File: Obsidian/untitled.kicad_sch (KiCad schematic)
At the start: 72 parts, among them U12 LP5951MF-3.0/NOPB, U13 LM336M-2.5, U14 DAC8550IDGK, U15 DAC8550IDGK, U16 CDCM61004RHB, U3 Si5351A-B-GT, Y1 OSC_25MHZ_RAKON_IVT3205CR, Y2 VM53S3-25.000-2.5/-30+75, Y3 OSC_20MHZ_IQD_LFVCXO026156, Y6 XTAL_25MHZ_TXC_8Y-25.000MAAJ-T

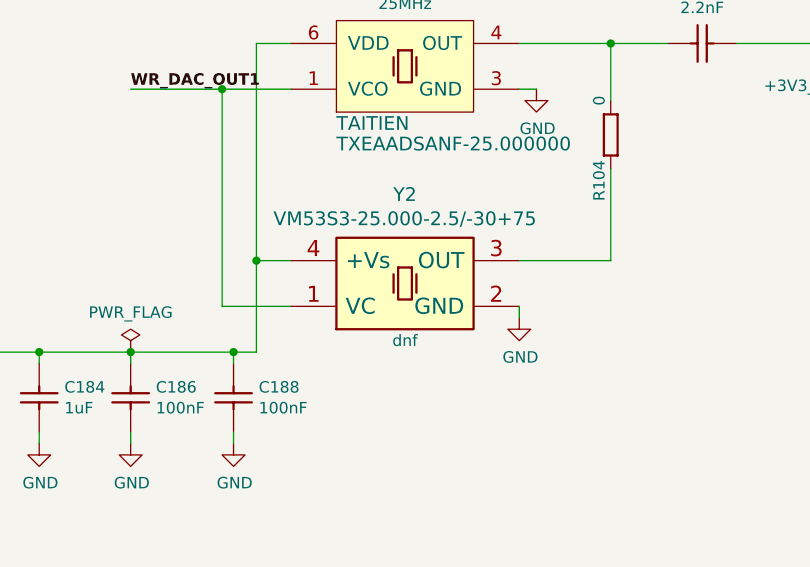
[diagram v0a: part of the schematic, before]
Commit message: update with available components on LCSC
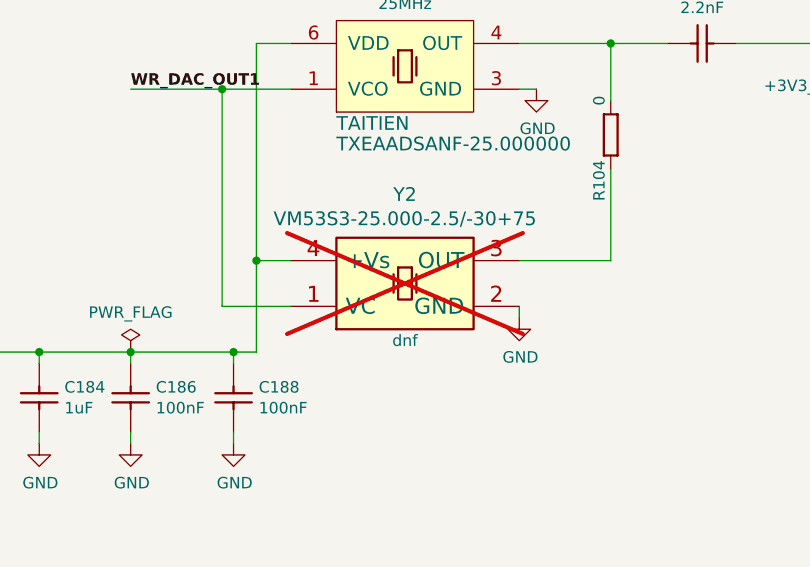
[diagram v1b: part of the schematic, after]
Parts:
- C182, C184, C207: LCSC (none) -> C29266
- C183, C185, C186, C188, C189, C190, C191, C194, C196, C197, C198, C206, C208, C209, C210, C211, C212, C215: LCSC (none) -> C190187
- C187, C192, C195, C199, C200, C201, C203: LCSC (none) -> C59461
- C193: LCSC (none) -> C1531
- C202, C204, C205, C213, C214, C248: LCSC (none) -> C110251
- L17, L18, L20: FT Rotation Offset (none) -> 0; LCSC (none) -> C113030
- R102, R103, R120, R121, R99: LCSC (none) -> C25094
- R104, R105, R106, R107, R108, R109, R110, R111, R112: LCSC (none) -> C106231
- R113, R116: LCSC (none) -> C351694
- R115, R117: LCSC (none) -> C413063
- R118, R119: LCSC (none) -> C114764
- R159: LCSC (none) -> C25111
- R162: LCSC (none) -> C25776
- R163, R176: LCSC (none) -> C60490
- U12: FT Rotation Offset (none) -> 270; LCSC (none) -> C2868982
- U13: FT Rotation Offset (none) -> 270; LCSC (none) -> C507207
- U14, U15: FT Rotation Offset (none) -> 270; LCSC (none) -> C524800
- U16: FT Rotation Offset (none) -> 0; LCSC (none) -> C524817
- U3: FT Rotation Offset (none) -> 0; LCSC (none) -> C504891
- Y1: LCSC (none) -> C52954962
- Y2: now not fitted
- Y3: FT Rotation Offset (none) -> 190; LCSC (none) -> C21547610
- Y6: FT Rotation Offset (none) -> 270; LCSC (none) -> C648942

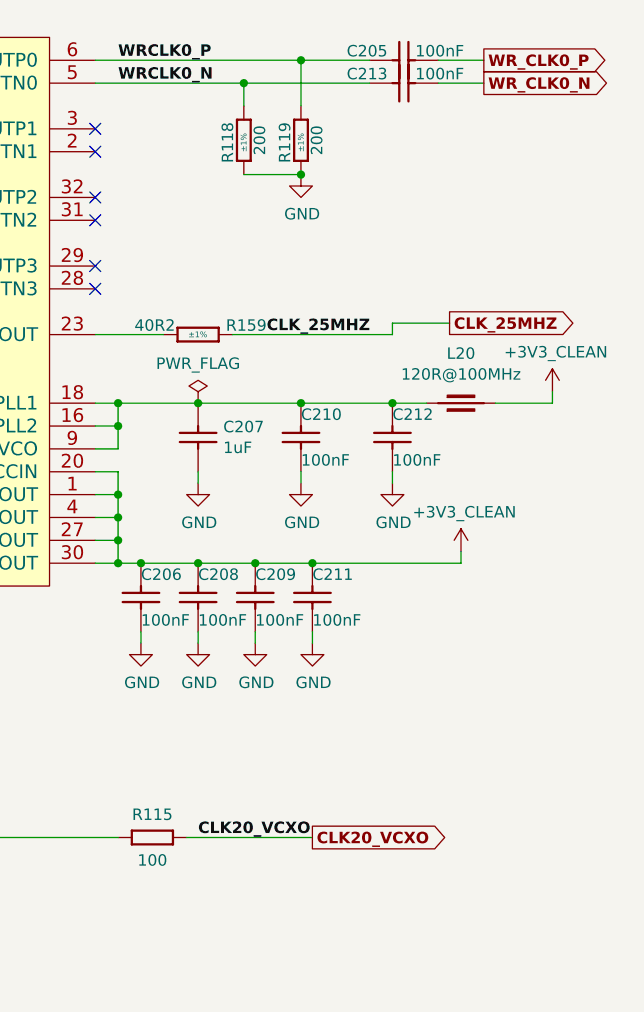
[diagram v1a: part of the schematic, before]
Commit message: adding wago
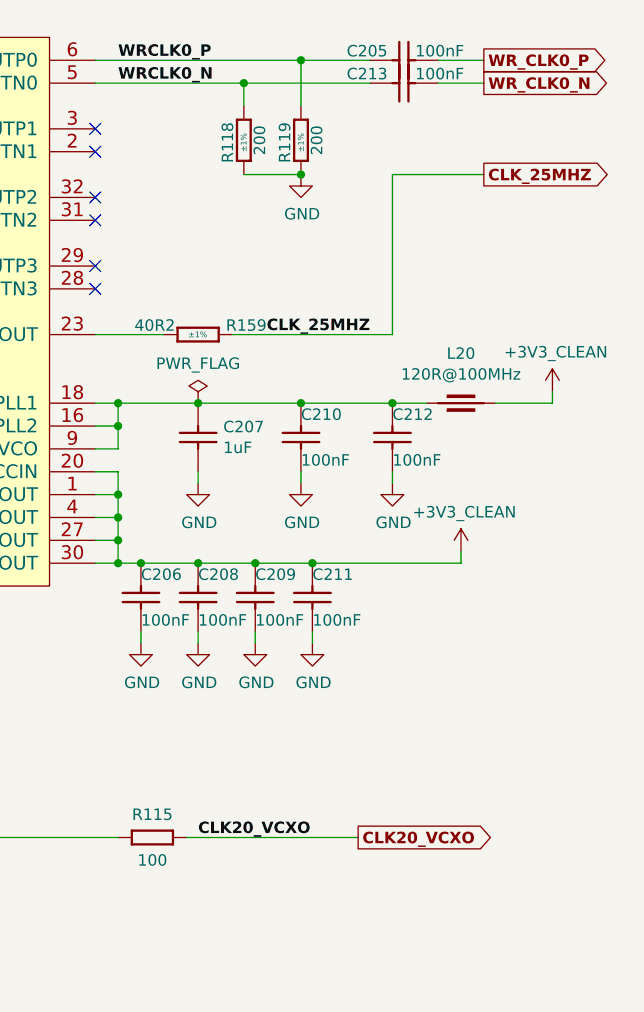
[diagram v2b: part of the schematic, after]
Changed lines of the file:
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@@
 	(wire
 		(pts
-			(xy 237.49 111.76) (xy 251.46 111.76)
+			(xy 237.49 111.76) (xy 256.54 111.76)
 		)
 		(stroke
@@
 	(wire
 		(pts
-			(xy 260.35 54.61) (xy 266.7 54.61)
+			(xy 260.35 38.1) (xy 270.51 38.1)
 		)
 		(stroke
@@
 	(wire
 		(pts
-			(xy 260.35 55.88) (xy 260.35 54.61)
+			(xy 260.35 55.88) (xy 260.35 38.1)
 		)
 		(stroke
@@
 	(global_label "CLK20_VCXO"
 		(shape output)
-		(at 251.46 111.76 0)
+		(at 256.54 111.76 0)
 		(fields_autoplaced yes)
 		(effects
@@
 		)
 		(property "Intersheetrefs" "${INTERSHEET_REFS}"
-			(at 266.7745 111.76 0)
+			(at 271.8545 111.76 0)
 			(effects
 				(font
@@
 	(global_label "CLK_25MHZ"
 		(shape output)
-		(at 266.7 54.61 0)
+		(at 270.51 38.1 0)
 		(fields_autoplaced yes)
 		(effects
@@
 		)
 		(property "Intersheetrefs" "${INTERSHEET_REFS}"
-			(at 281.1073 54.61 0)
+			(at 284.9173 38.1 0)
 			(effects
 				(font
@@
 			)
 		)
+	)
+	(rule_area
+		(polyline
+			(pts
+				(xy 269.24 22.86) (xy 269.24 41.91) (xy 284.48 41.91) (xy 284.48 22.86)
+			)
+			(stroke
+				(width 0)
+				(type dash)
+			)
+			(fill
+				(type none)
+			)
+		)
+	)
+	(rule_area
+		(polyline
+			(pts
+				(xy 255.27 107.95) (xy 255.27 163.83) (xy 274.32 163.83) (xy 274.32 107.95)
+			)
+			(stroke
+				(width 0)
+				(type dash)
+			)
+			(fill
+				(type none)
+			)
+		)
+	)
+	(netclass_flag ""
+		(length 2.54)
+		(shape round)
+		(at 264.16 107.95 0)
+		(fields_autoplaced yes)
+		(effects
+			(font
+				(size 1.27 1.27)
+			)
+			(justify left bottom)
+		)
+		(property "Netclass" "CLK"
+			(at 264.8585 105.41 0)
+			(effects
+				(font
+					(size 1.27 1.27)
+				)
+				(justify left)
+			)
+		)
+		(property "Component Class" ""
+			(at -49.53 72.39 0)
+			(effects
+				(font
+					(size 1.27 1.27)
+					(italic yes)
+				)
+			)
+		)
+	)
+	(netclass_flag ""
+		(length 2.54)
+		(shape round)
+		(at 276.86 22.86 0)
+		(fields_autoplaced yes)
+		(effects
+			(font
+				(size 1.27 1.27)
+			)
+			(justify left bottom)
+		)
+		(property "Netclass" "CLK"
+			(at 277.5585 20.32 0)
+			(effects
+				(font
+					(size 1.27 1.27)
+				)
+				(justify left)
+			)
+		)
+		(property "Component Class" ""
+			(at -36.83 -12.7 0)
+			(effects
+				(font
+					(size 1.27 1.27)
+					(italic yes)
+				)
+			)
+		)

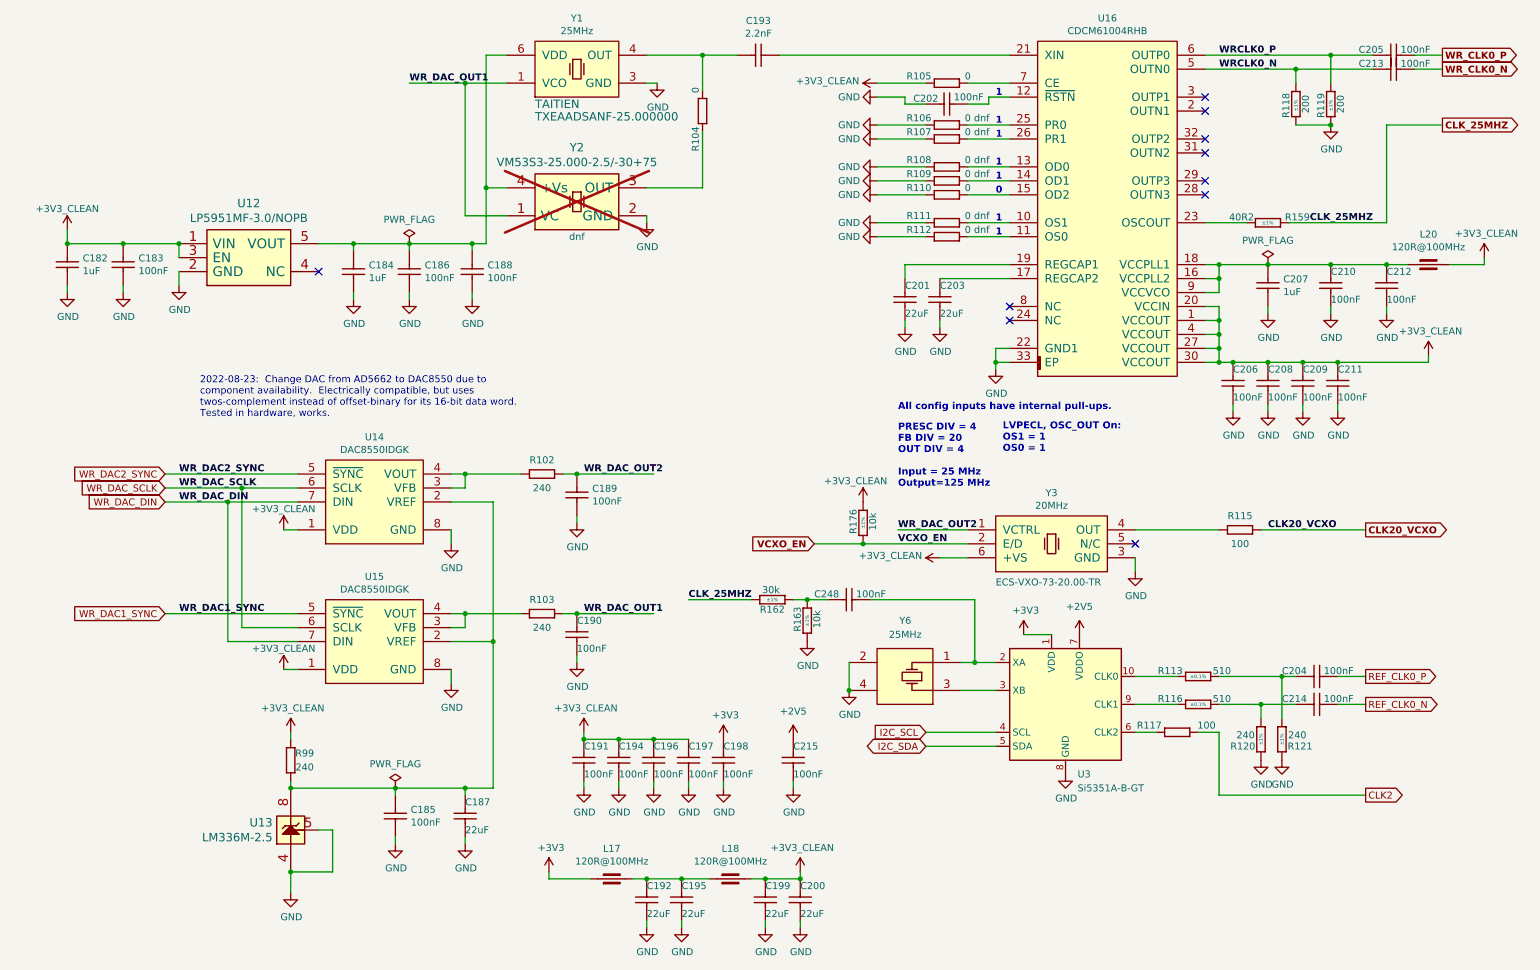
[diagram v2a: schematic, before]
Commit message: replacing global label with hierarchical label
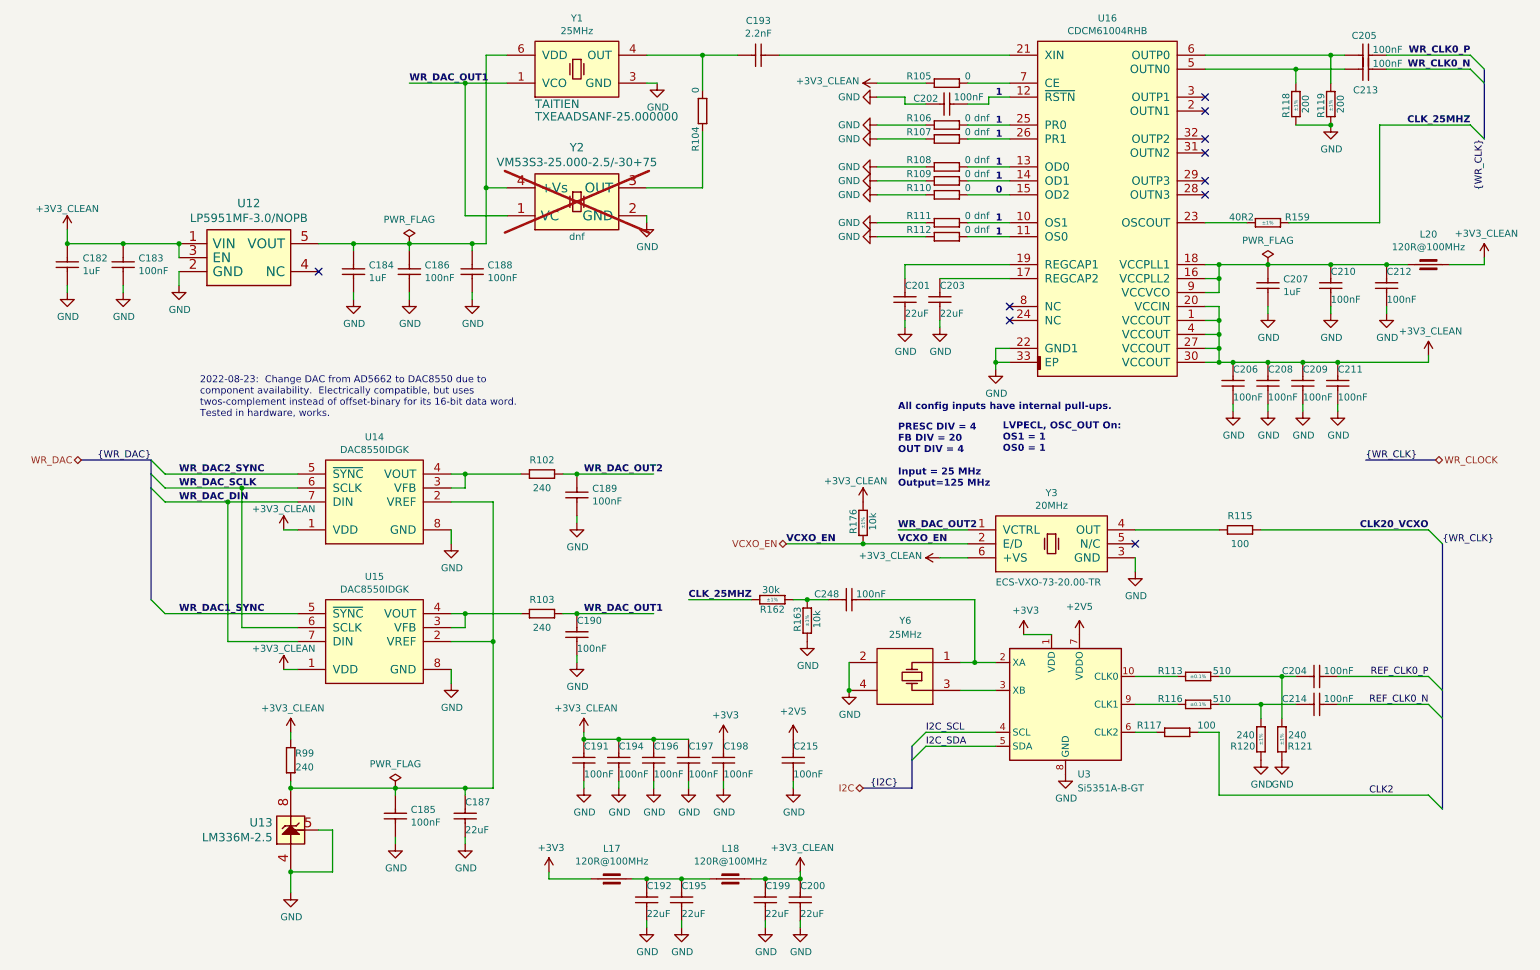
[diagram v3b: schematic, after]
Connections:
- net WRCLK0_N: no longer names the net of C213.2, R118.1, U16.5 (OUTN0)
- net WRCLK0_P: no longer names the net of C205.2, R119.1, U16.6 (OUTP0)
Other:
- moved on the sheet: C205, C213

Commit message: Adding symbol library
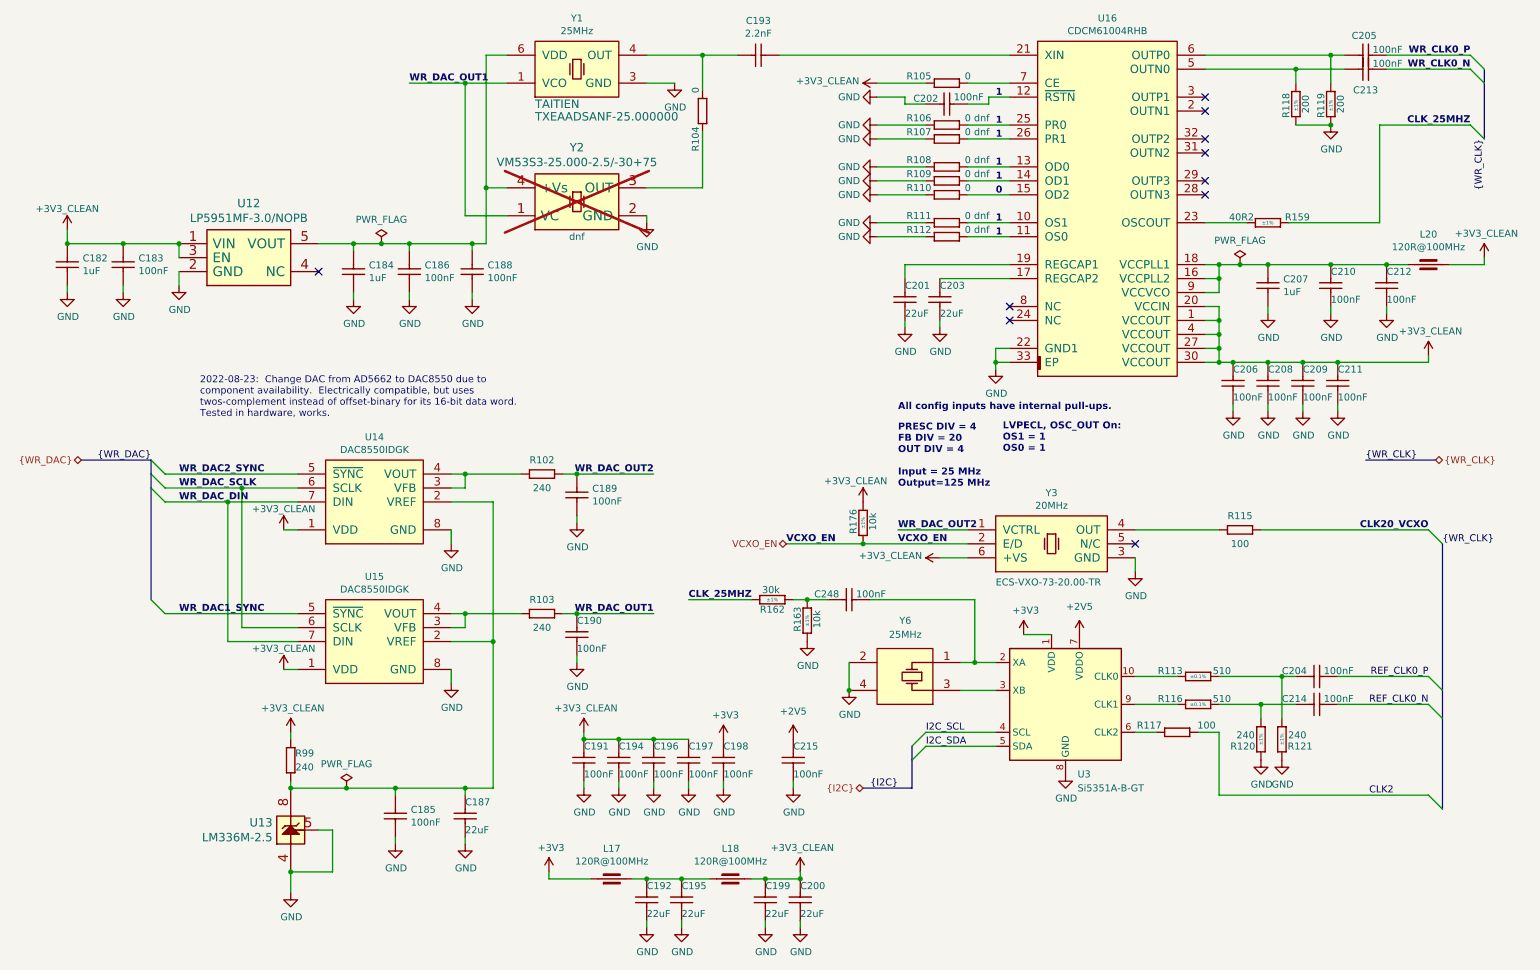
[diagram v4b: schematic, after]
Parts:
- C182, C184, C207: symbol Capacitors_SMD:CC0402_1UF_16V_10%_X5R -> Library_Symbol:CC0402_1UF_16V_10%_X5R
- C183, C185, C186, C188, C189, C190, C191, C194, C196, C197, C198, C206, C208, C209, C210, C211, C212, C215: symbol Capacitors_SMD:CC0201_100NF_6.3V_10%_X5R -> Library_Symbol:CC0201_100NF_6.3V_10%_X5R
- C187, C192, C195, C199, C200, C201, C203: symbol Capacitors_SMD:CC0603_22UF_6.3V_20%_X5R -> Library_Symbol:CC0603_22UF_6.3V_20%_X5R
- C193: symbol Capacitors_SMD:CC0402_2.2NF_50V_10%_X7R -> Library_Symbol:CC0402_2.2NF_50V_10%_X7R
- C202, C204, C205, C213, C214, C248: symbol Capacitors SMD:CC0402_100NF_50V_10%_X7R -> Library_Symbol:CC0402_100NF_50V_10%_X7R
- L17, L18, L20: symbol Inductors_SMD:IND0603_MURATA_BLM18SG121TN1D -> Library_Symbol:IND0603_MURATA_BLM18SG121TN1D
- R102, R103, R99: symbol Resistors_SMD:R0402_240R_1%_0.0625W_100PPM -> Library_Symbol:R0402_240R_1%_0.0625W_100PPM
- R104, R105, R106, R107, R108, R109, R110, R111, R112: symbol Resistors_SMD:R0402_0R_JUMPER -> Library_Symbol:R0402_0R_JUMPER
- R113, R116: symbol Resistors SMD:R0402_510R_0.1%_0.0625W_10PPM -> Library_Symbol:R0402_510R_0.1%_0.0625W_10PPM
- R115, R117: symbol Resistors_SMD:R0402_100R_1%_0.1W_100PPM -> Library_Symbol:R0402_100R_1%_0.1W_100PPM
- R118, R119: symbol Resistors SMD:R0402_200R_1%_0.0625W_100PPM -> Library_Symbol:R0402_200R_1%_0.0625W_100PPM
- R120, R121: symbol Resistors SMD:R0402_240R_1%_0.0625W_100PPM -> Library_Symbol:R0402_240R_1%_0.0625W_100PPM
- R159: symbol Resistors SMD:R0402_40R2_1%_0.0625W_100PPM -> Library_Symbol:R0402_40R2_1%_0.0625W_100PPM
- R162: symbol Resistors SMD:R0402_30K_1%_0.0625W_100PPM -> Library_Symbol:R0402_30K_1%_0.0625W_100PPM
- R163, R176: symbol Resistors SMD:R0402_10K_1%_0.0625W_100PPM -> Library_Symbol:R0402_10K_1%_0.0625W_100PPM
- U12: symbol marble_misc:LP5951-clocks-SchDoc-cache -> Library_Symbol:LP5951-clocks-SchDoc-cache
- U13: symbol marble_misc:LM336M-2.5-clocks-SchDoc-cache -> Library_Symbol:LM336M-2.5-clocks-SchDoc-cache
- U14, U15: symbol Analog_&_Interface:DAC8550IDGK -> Library_Symbol:DAC8550IDGK
- U16: symbol Logic:CDCM61004RHB -> Library_Symbol:CDCM61004RHB
- U3: symbol Oscillator:Si5351A-B-GT -> Library_Symbol:Si5351A-B-GT
- Y1: symbol Crystals_&_Oscillators:OSC_25MHZ_RAKON_IVT3205CR -> Library_Symbol:OSC_25MHZ_RAKON_IVT3205CR
- Y2: symbol marble_misc:Oscillator_1VC_2GND_3OUT_4+Vs-clocks-SchDoc-cache -> Library_Symbol:Oscillator_1VC_2GND_3OUT_4+Vs-clocks-SchDoc-cache
- Y3: symbol Crystals_&_Oscillators:OSC_20MHZ_IQD_LFVCXO026156 -> Library_Symbol:OSC_20MHZ_IQD_LFVCXO026156
- Y6: symbol Crystals & Oscillators:XTAL_25MHZ_TXC_8Y-25.000MAAJ-T -> Library_Symbol:XTAL_25MHZ_TXC_8Y-25.000MAAJ-T

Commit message: Correct Schematic errors
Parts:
- C182, C184, C193, C202, C204, C205, C207, C213, C214, C248: footprint Capacitors SMD:CAPC1005X55N -> Footprint:CAPC1005X55N
- C183, C185, C186, C189, C190, C191, C194, C196, C197, C198, C206, C208, C209, C210, C211, C212, C215: footprint Capacitors SMD:CAPC0603X33N -> Footprint:CAPC0603X33N
- C187, C192, C195, C199, C200, C201, C203: footprint CAPC1709X100N -> Footprint:CAPC1709X100N
- C188: footprint Capacitors SMD:CAPC0603X33N -> Footprint:CAPC1005X55N
- L17, L18, L20: footprint INDC1608X65N -> Footprint:INDC1608X65N
- R102, R103, R113, R116, R118, R119, R120, R121, R159, R162, R163, R176, R99: footprint Resistors SMD:RESC1005X40N -> Footprint:RESC1005X40N
- R104, R105, R106, R107, R108, R109, R110, R111, R112, R115, R117: footprint RESC1005X40N -> Footprint:RESC1005X40N; Database Table Name (none) -> Resistors; Footprint Library (none) -> Resistors SMD; HelpURL (none) -> \\cern.ch\dfs\Applications\Altium\Datasheets\R0402_Phycomp_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
- U12: footprint ICs And Semiconductors SMD:SOT95P284X122-5N -> Footprint:SOT95P284X122-5N
- U13: footprint ICs And Semiconductors SMD:SOIC127P600X175-8N -> Footprint:SOIC127P600X175-8N
- U14, U15: footprint ICs And Semiconductors SMD:SOP65P490X110-8N -> Footprint:SOP65P490X110-8N
- U16: footprint ICs And Semiconductors SMD:QFN50P500X500X100-33N-S355 -> Footprint:QFN50P500X500X100-33N-S355
- U3: footprint Package_SO:MSOP-10_3x3mm_P0.5mm -> Footprint:MSOP-10_3x3mm_P0.5mm
- Y1: footprint ICs And Semiconductors SMD:OSC_ABRACON_ASEMPC -> Footprint:OSC_ABRACON_ASEMPC
- Y2: footprint ICs And Semiconductors SMD:OSCCC320X500X160-4N -> Footprint:OSCCC320X500X160-4N
- Y3: footprint ICs And Semiconductors SMD:OSC_IQD_CFPV-45 -> Footprint:OSC_IQD_CFPV-45
- Y6: footprint ICs And Semiconductors SMD:XTAL_TXC_8Y -> Footprint:XTAL_TXC_8Y
